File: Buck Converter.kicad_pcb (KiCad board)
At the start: 2 copper layers, 55.9 x 27.9 mm, 10 parts, among them J1 Screw_Terminal_01x02, J2 Screw_Terminal_01x02, U1 LM2576S-ADJ

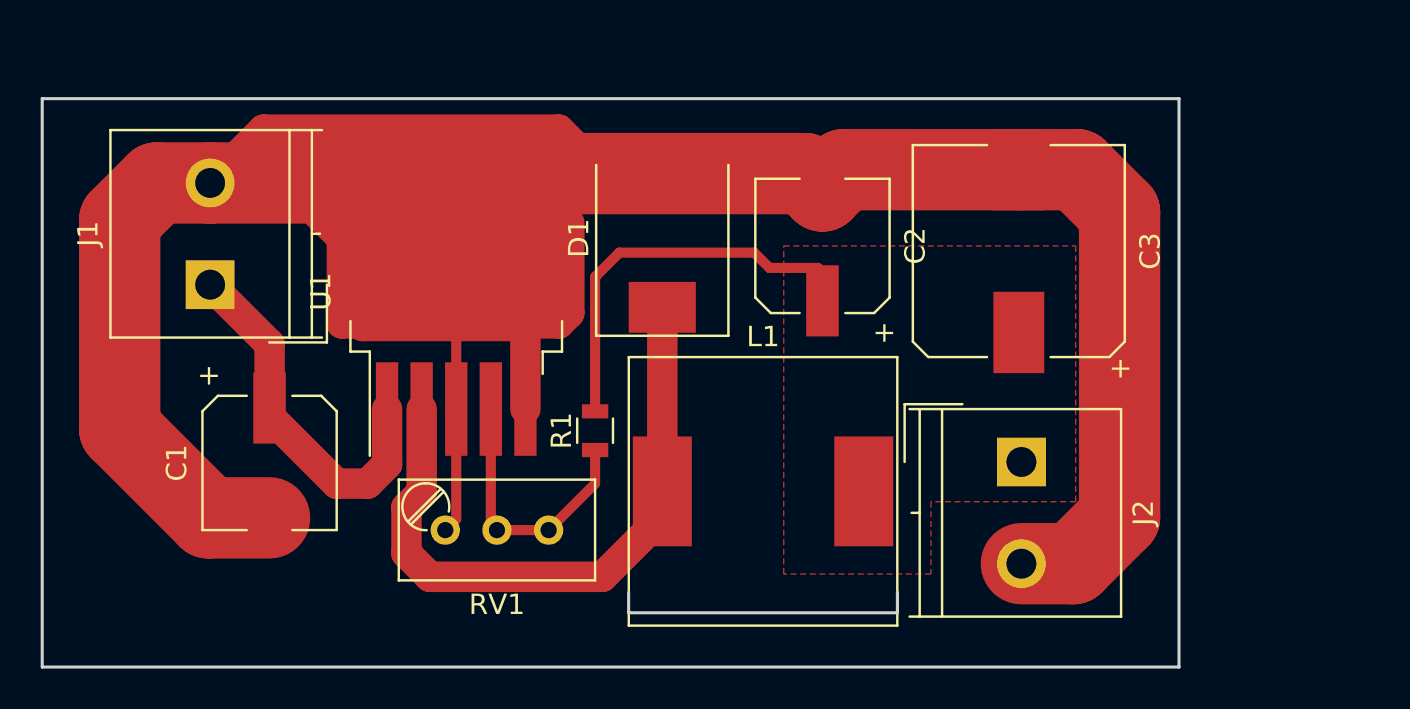
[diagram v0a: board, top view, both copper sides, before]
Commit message: Start of modifications for Through Hole version
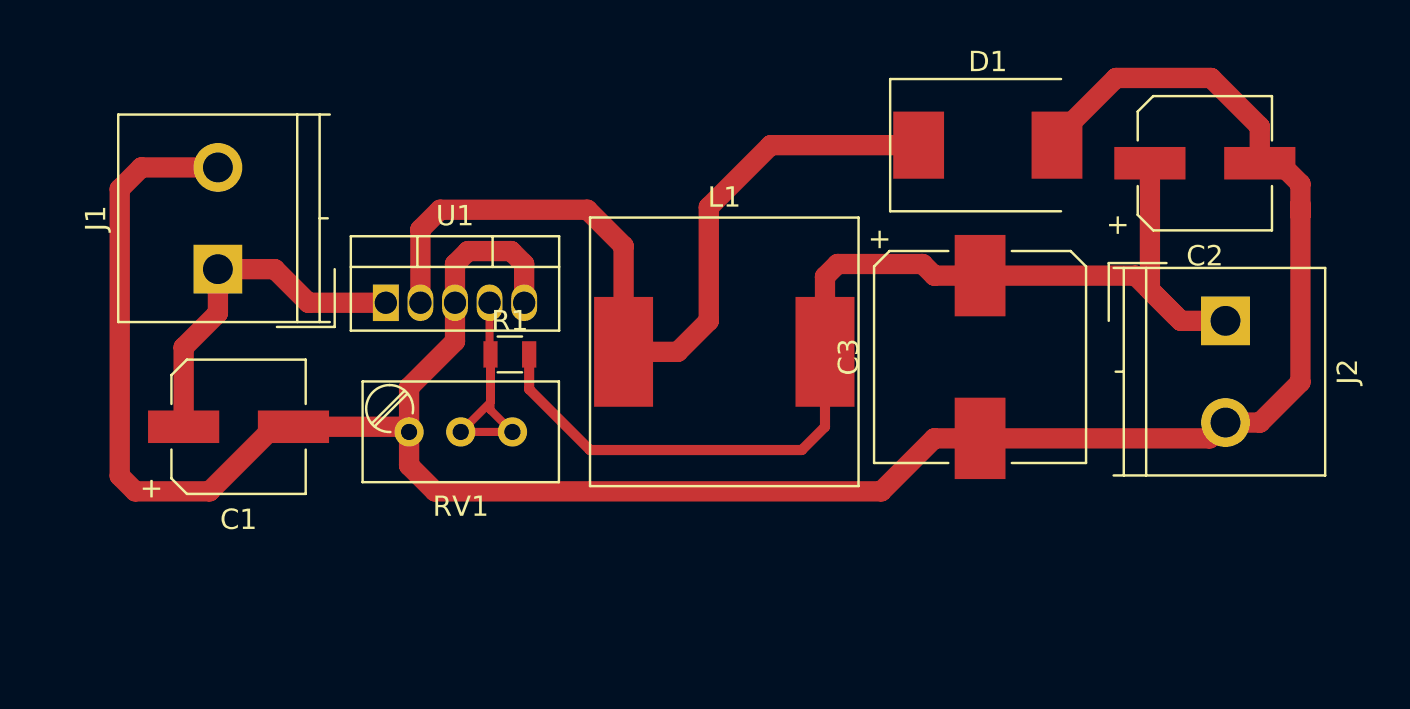
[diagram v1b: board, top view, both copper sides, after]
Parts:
- U1: footprint TO_SOT_Packages_SMD:TO-263-5_TabPin3 -> Package_TO_SOT_THT:TO-220-5_Vertical
- moved C2 19.2 mm to (138.4, 65.4), turned to 0 degrees
- moved D1 16.6 mm to (127.8, 64.5), turned to 0 degrees
- moved J2 12.2 mm to (139.4, 73.2)
- moved L1 7.12 mm to (114.8, 74.7)
- moved R1 5.62 mm to (104.3, 74.8), turned to 0 degrees
- moved C3 5.54 mm to (127.4, 74.9), turned to 270 degrees
- moved RV1 5.14 mm to (99.3, 78.6)
- moved U1 3.50 mm to (98.2, 72.3), turned to 0 degrees
- moved C1 2.34 mm to (90.9, 78.4), turned to 0 degrees
- moved J1 0.85 mm to (89.9, 70.6)
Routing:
- net GND: track 189.7 -> 125.6 mm
- net /VOUT: track 20.1 -> 54.5 mm
- net Net-(D1-Pad1): track 32.0 -> 41.9 mm
- net VCC: track 17.9 -> 17.4 mm
- removed copper zone on F.Cu, net /VOUT
- removed copper zone on F.Cu, net GND
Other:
- board outline removed
